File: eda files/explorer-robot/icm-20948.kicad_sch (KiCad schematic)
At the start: 2 parts, among them U3 ICM-20948, U4 TXB0108PW

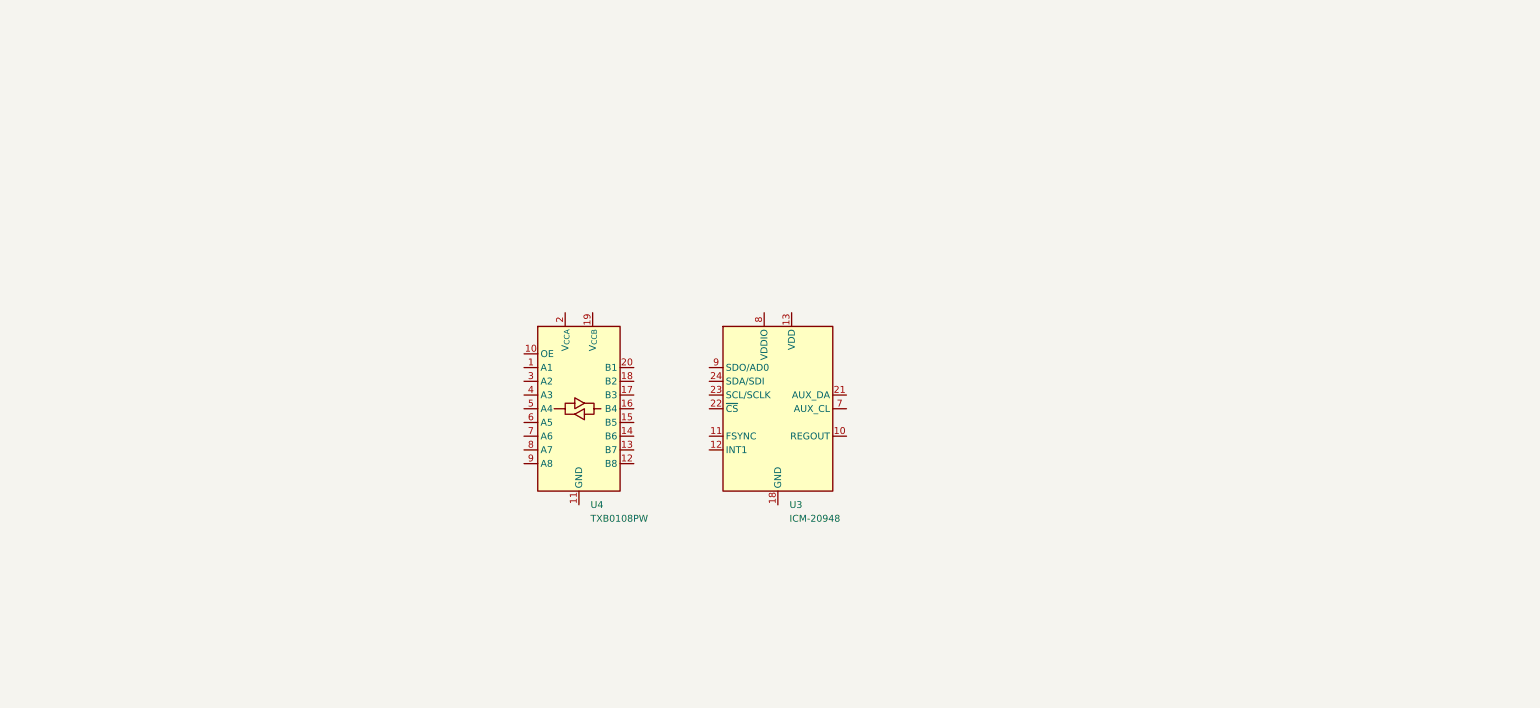
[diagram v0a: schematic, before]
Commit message: finish schematic for ICM-20948; requiring changes to pin assignment
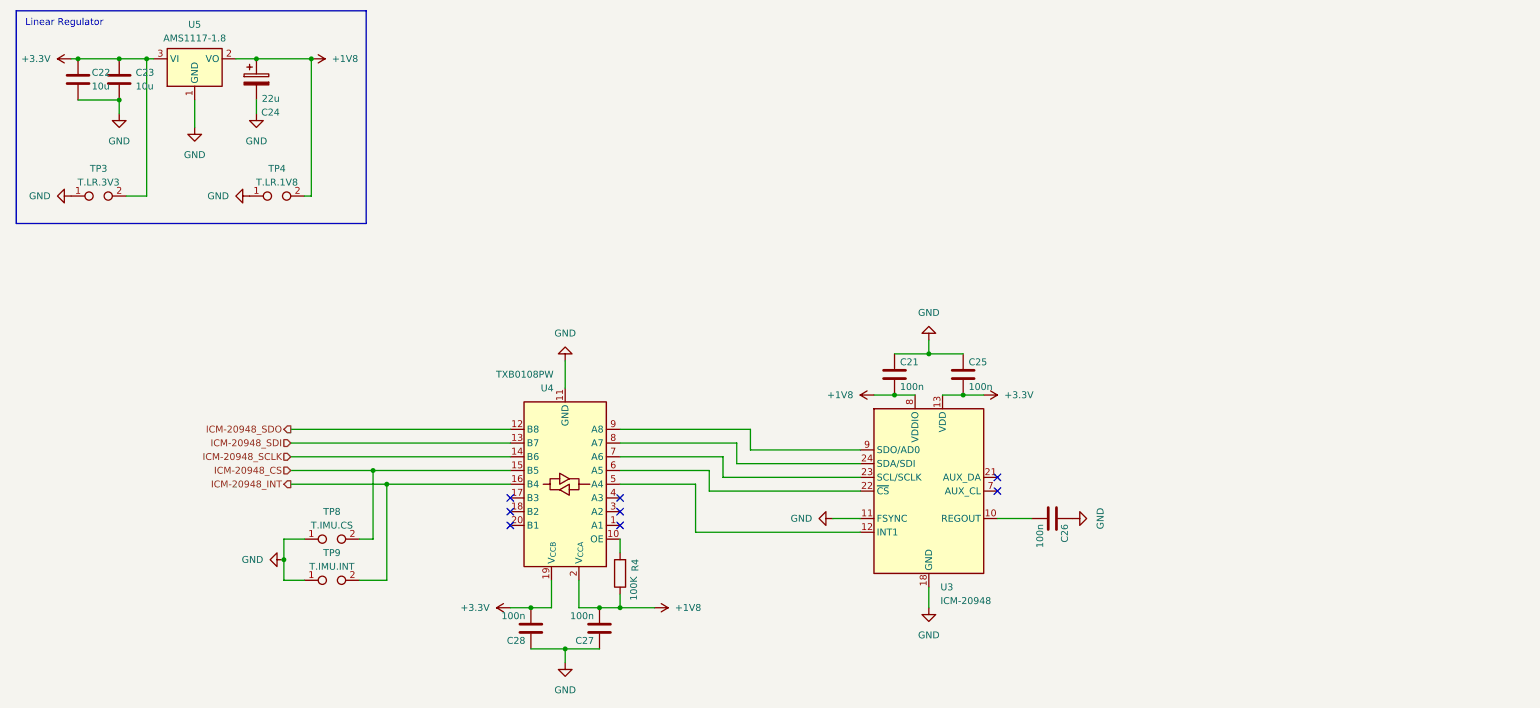
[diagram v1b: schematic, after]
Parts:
- added C21, C25, C26, C27, C28: 100n, Capacitor_SMD:C_0201_0603Metric, symbol Device:C
- added C22, C23: 10u, Capacitor_SMD:C_0201_0603Metric, symbol Device:C
- added C24: 22u, Capacitor_Tantalum_SMD:CP_EIA-3216-18_Kemet-A, symbol Device:C_Polarized
- added R4: 100K, Resistor_SMD:R_01005_0402Metric, symbol Device:R
- added TP3: T.LR.3V3, tp:TestPoint_Bridge_Pitch3.81mm_Drill1.3mm, symbol Connector:TestPoint_2Pole
- added TP4: T.LR.1V8, tp:TestPoint_Bridge_Pitch3.81mm_Drill1.3mm, symbol Connector:TestPoint_2Pole
- added TP8: T.IMU.CS, tp:TestPoint_Bridge_Pitch3.81mm_Drill1.3mm, symbol Connector:TestPoint_2Pole
- added TP9: T.IMU.INT, tp:TestPoint_Bridge_Pitch3.81mm_Drill1.3mm, symbol Connector:TestPoint_2Pole
- added U5: AMS1117-1.8, Package_TO_SOT_SMD:SOT-223-3_TabPin2, symbol Regulator_Linear:AMS1117-3.3
- U3: MFR (none) -> TDK InvenSense; MPN (none) -> ICM-20948
- U4: MFR (none) -> Texas Instruments; MPN (none) -> TXB0108PWR
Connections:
- net at U3.10 (REGOUT): now also C26.2
- net GND: now reaches U3.11 (FSYNC)
- net GND: now also U3.18 (GND), U3.20 (GND), U4.11 (GND), C21.1, C22.2, C23.2, C24.2, C25.1, C26.1, C27.1, C28.1, TP3.1, TP4.1, TP8.1, TP9.1, U5.1 (GND)
- net at U3.12 (INT1): now also U4.5 (A4)
- net +3.3V: now reaches U3.13 (VDD)
- net +3.3V: now also U4.19 (V_{CCB}), C22.1, C23.1, C25.2, C28.2, TP3.2, U5.3 (VI)
- net at U3.22 (~{CS}): now also U4.6 (A5)
- net at U3.23 (SCL/SCLK): now also U4.7 (A6)
- net at U3.24 (SDA/SDI): now also U4.8 (A7)
- net +1V8: now reaches U3.8 (VDDIO)
- net +1V8: now also U4.2 (V_{CCA}), C21.2, C24.1, C27.2, R4.1, TP4.2, U5.2 (VO)
- net at U3.9 (SDO/AD0): now also U4.9 (A8)
- net at U4.10 (OE): now also R4.2
- net ICM-20948_SDO: now reaches U4.12 (B8)
- net ICM-20948_SDI: now reaches U4.13 (B7)
- net ICM-20948_SCLK: now reaches U4.14 (B6)
- net ICM-20948_CS: now reaches U4.15 (B5)
- net ICM-20948_CS: now also TP8.2
- net ICM-20948_INT: now reaches U4.16 (B4)
- net ICM-20948_INT: now also TP9.2
- no-connect marks 0 -> 8
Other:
- note added: "Linear Regulator"
- title: (none) -> ICM-20948 and supporting components
- moved on the sheet: U3, U4

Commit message: Split power and motor driver into dedicated schematic sheets
Add ADRs 0018–0020 covering ground topology, battery rail and
connector protection decisions. Move battery, 5 V buck and test points
to a new power_and_batt sheet, and the TB6612FNG with motor connectors
to a new tb6612fng sheet.

Collapse the single ground net at the TB6612FNG, add the three-tier VM
decoupling stack and bidirectional TVS clamps on the motor pairs and VM.
Switch the 5 V rail to a TPS5430DDAR with a 220 µF/25 V polymer bulk
shared across the battery, VM and 5 V rails. Fix the ICM-20948 regulator
symbol to AMS1117-1.8.
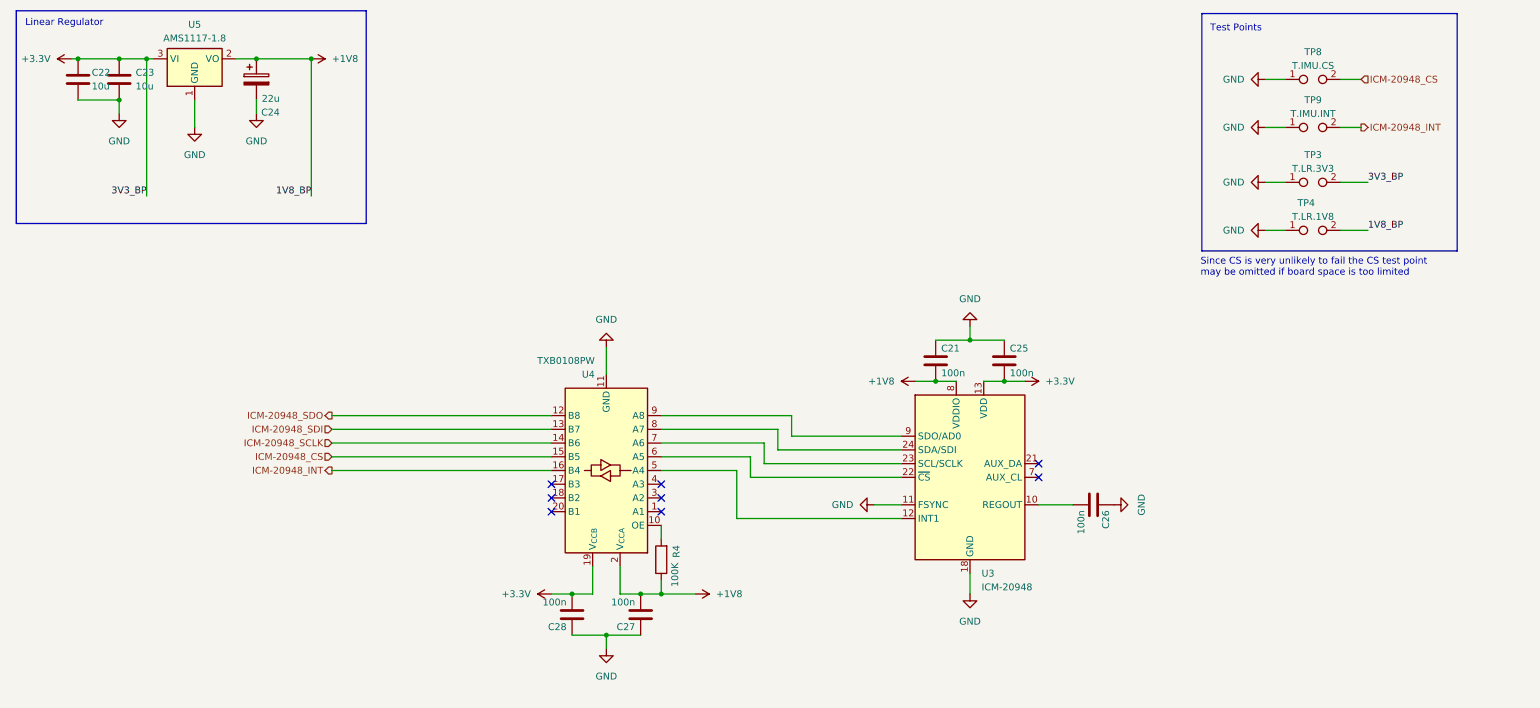
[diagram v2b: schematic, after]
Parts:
- C21, C22, C23, C25, C26, C27, C28: footprint Capacitor_SMD:C_0201_0603Metric -> Capacitor_SMD:C_0603_1608Metric
- R4: footprint Resistor_SMD:R_01005_0402Metric -> Resistor_SMD:R_0402_1005Metric
- U5: symbol Regulator_Linear:AMS1117-3.3 -> Regulator_Linear:AMS1117-1.8
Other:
- note added: "Since CS is very unlikely to fail the CS test point may be omitted if board space is too limited"
- note added: "Test Points"
- moved on the sheet: C21, C25, C26, C27, C28, R4, U3, U4

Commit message: place test points, tidy up, ERC
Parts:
- removed TP3: T.LR.3V3, tp:TestPoint_Bridge_Pitch3.81mm_Drill1.3mm, symbol Connector:TestPoint_2Pole
- TP4, TP8, TP9: footprint tp:TestPoint_Bridge_Pitch3.81mm_Drill1.3mm -> Connector_PinHeader_2.54mm:PinHeader_1x02_P2.54mm_Vertical
- U3: footprint Sensor_Motion:InvenSense_QFN-24_3x3mm_P0.4mm -> easyeda imports:QFN-24_L3.0-W3.0-P0.40-BL-EP
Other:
- note removed: "Since CS is very unlikely to fail the CS test point may be omitted if board space is too limited"
- moved on the sheet: TP4

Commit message: Update AI camera branch to 5V and document schematic
- ADR-0027 supersedes ADR-0025: AI camera input is 5V, not 3.3V
- Move U9 VIN and C55 back to +5V in aicam.kicad_sch
- Update CONTEXT.md branch descriptions and ADR cross-references
- Record ICM-20948 placement status and corrected battery divider ratio
- Adjust battery_charge_read for 33k/10k divider (0.2326 ratio)
- Enable sheet component classes; refresh netlist and PCB footprints
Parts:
- added R45: 150, Resistor_SMD:R_0603_1608Metric, symbol Device:R
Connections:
- net +1V8: now also C25.2, U3.13 (VDD), R45.1
- net +3.3V: no longer C25.2, U3.13 (VDD)
- net GND: now also R45.2

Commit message: Add CS pull-up and reset-before-verify for ICM-20948
R46 (2.2 kΩ) holds ICM-20948_CS high on the MCU side so the IMU
stays deselected through RP2350 reset, when Bank 0 GPIOs are pulled
low. Firmware now constructs the driver without detection, resets via
init(), then verifies WHO_AM_I inside the retry loop as defence in
depth. Documents the rationale in ADR-0017 and updates CONTEXT.md.
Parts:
- added R46: 2K2, Resistor_SMD:R_0603_1608Metric, symbol Device:R
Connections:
- net +3.3V: now also R46.2
- net GND: now also U4.1 (A1), U4.17 (B3), U4.18 (B2), U4.20 (B1), U4.3 (A2), U4.4 (A3)
- net ICM-20948_CS: now also R46.1
- no-connect marks 8 -> 2
